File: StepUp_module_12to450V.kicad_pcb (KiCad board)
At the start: 2 copper layers, 81.8 x 47.2 mm, 37 parts, among them J1 Screw_Terminal_01x04, Q1 HY1707, Q2 HY1707, Q3 S8050, U1 UC3845

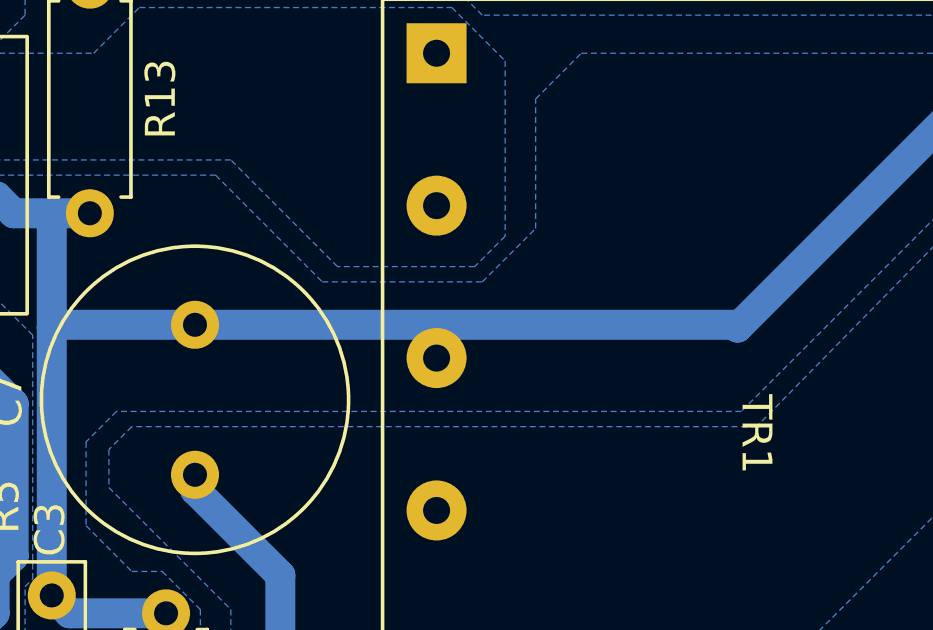
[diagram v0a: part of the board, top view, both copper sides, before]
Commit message: Fixed ci and kibot_main, fixed DRC issue
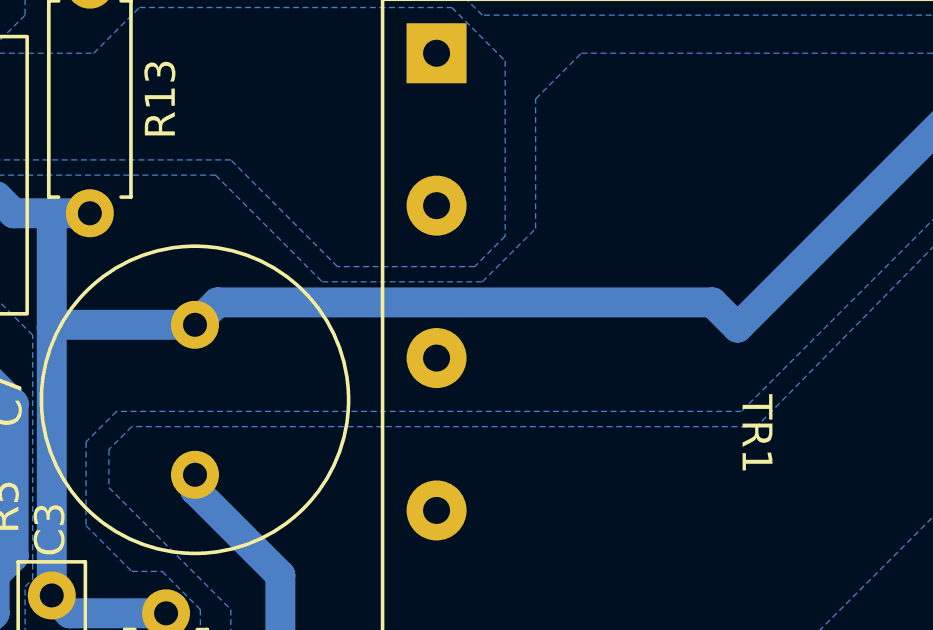
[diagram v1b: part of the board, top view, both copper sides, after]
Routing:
- net GND: track 195.7 -> 196.3 mm
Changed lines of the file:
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@@
-	)
-	(segment
-		(start 166.355 74.6)
-		(end 166.262677 74.507677)
-		(width 1)
-		(layer "B.Cu")
-		(net 15)
 	)
 	(segment
@@
 	)
 	(segment
-		(start 166.262677 74.507677)
-		(end 148.269496 74.507677)
+		(start 165.5166 73.7616)
+		(end 149.015573 73.7616)
 		(width 1)
 		(layer "B.Cu")
@@
 	)
 	(segment
-		(start 179.055 61.9)
-		(end 166.355 74.6)
-		(width 1)
-		(layer "B.Cu")
-		(net 15)
-	)
-	(segment
 		(start 144.09 84.125)
 		(end 143.495 83.53)
@@
 	)
 	(segment
-		(start 179.055 56.185)
-		(end 179.055 61.9)
+		(start 121.4 71.45)
+		(end 121.425 71.425)
 		(width 1)
 		(layer "B.Cu")
@@
 	)
 	(segment
-		(start 121.4 71.45)
-		(end 121.425 71.425)
+		(start 149.015573 73.7616)
+		(end 148.269496 74.507677)
+		(width 1)
+		(layer "B.Cu")
+		(net 15)
+	)
+	(segment
+		(start 166.355 74.6)
+		(end 165.5166 73.7616)
 		(width 1)
 		(layer "B.Cu")
@@
 	)
 	(segment
+		(start 179.055 56.185)
+		(end 179.055 61.9)
+		(width 1)
+		(layer "B.Cu")
+		(net 15)
+	)
+	(segment
 		(start 147.305 84.125)
 		(end 144.09 84.125)
@@
 		(width 1)
 		(layer "B.Cu")
+		(net 15)
+	)
+	(segment
+		(start 179.055 61.9)
+		(end 166.355 74.6)
+		(width 1)
+		(layer "B.Cu")
